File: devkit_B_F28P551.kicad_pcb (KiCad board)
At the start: 2 copper layers, 28 x 75 mm, 27 parts, among them J1 DEVKIT_C2000_ROW_A, J2 DEVKIT_C2000_ROW_B, J3 Tag-Connect-2050_10, J4 RESET, U1 TMS320F28P551SG5PM, U2 MCP1700-3302E/TT, U3 MCP1700-3302E/TT

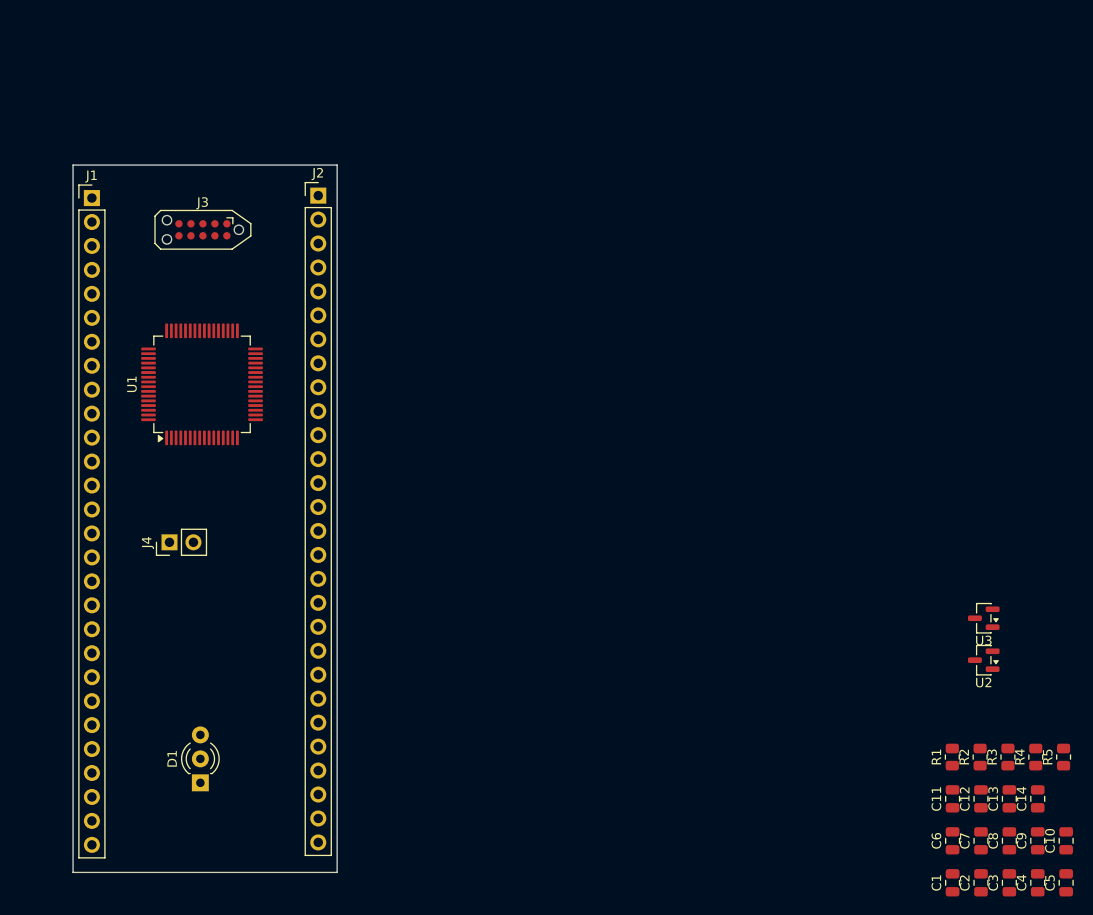
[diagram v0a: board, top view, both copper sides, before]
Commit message: Devkit B routé, sérigraphie des connecteurs 2x28 et logo
Placement/routage complet du PCB devkit B (24 empreintes, J1/J2 câblés).
Étiquettes de sérigraphie ajoutées sur les 56 broches des connecteurs
Row A/Row B (canal ADC réel, GPIO, rôle de bus générique, alimentations)
via kipy sur l'instance ouverte, plutôt que les noms spécialisés du
schéma. Logo ajouté (lib/lebel-logo) et fp-lib-table versionné.

Co-Authored-By: Claude Sonnet 5 <noreply@anthropic.com>
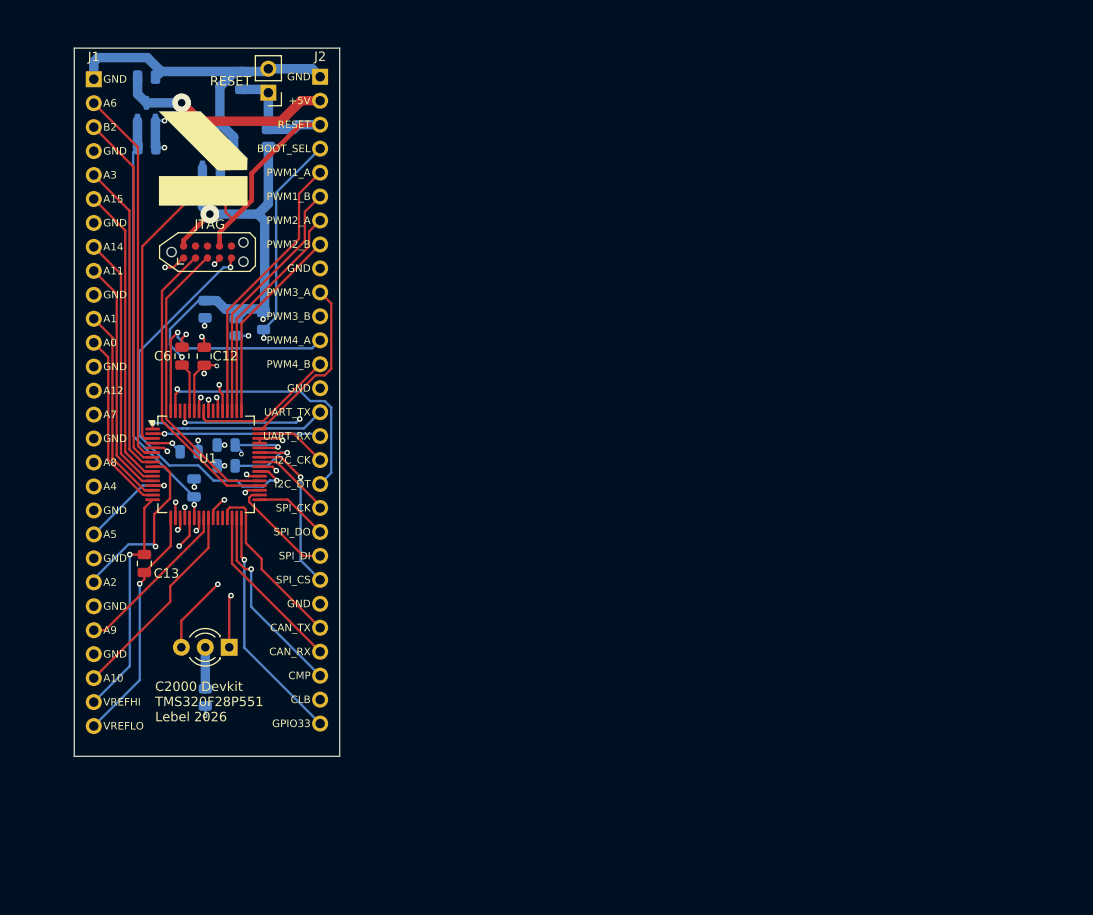
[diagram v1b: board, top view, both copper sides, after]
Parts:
- removed C7: 2u2, Capacitor_SMD:C_0805_2012Metric
- removed C9: 100n, Capacitor_SMD:C_0805_2012Metric
- removed J3: Tag-Connect-2050_10, Connector:Tag-Connect_TC2050-IDC-NL_2x05_P1.27mm_Vertical
- added G***: LOGO, lib:lebel-logo, F.Cu at (137.6, 55.8)
- added JTAG: Tag-Connect-2050_10, Connector:Tag-Connect_TC2050-IDC-NL_2x05_P1.27mm_Vertical, F.Cu at (137.8, 65.7)
- C1, C10, C11, C14, C2, C3, C4, C5, C8, J1, J2, R1, R2, R3, R4, R5, U2, U3: moved to B.Cu
- moved C3 125.2 mm to (131.3, 47.2), turned to 0 degrees
- moved C4 122.5 mm to (131.3, 54.7), turned to 0 degrees
- moved C14 113.7 mm to (141.4, 47.5)
- moved C1 112.6 mm to (138.1, 52.1), turned to 0 degrees
- moved C2 109.5 mm to (138.2, 59.6), turned to 0 degrees
- moved U3 103.8 mm to (131.3, 50.8), turned to 90 degrees
- moved C10 101.7 mm to (135.8, 86.9), turned to 0 degrees
- moved R2 100.0 mm to (144.2, 53.6), turned to -90 degrees
- moved C5 99.4 mm to (139.7, 88.4), turned to 180 degrees
- moved U2 97.6 mm to (138.2, 55.8), turned to 90 degrees
- moved C6 96.5 mm to (135.1, 76.8)
- moved R4 96.3 mm to (140.8, 73.7)
- moved C13 95.0 mm to (131.1, 98.8), turned to -90 degrees
- moved C12 94.8 mm to (137.4, 76.8)
- moved C8 94.2 mm to (136.3, 90.7)
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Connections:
- J1 pad 1: unconnected-(J1-GND-Pad1) -> GND
- J1 pad 10: unconnected-(J1-GND-Pad10) -> GND
- J1 pad 13: unconnected-(J1-GND-Pad13) -> GND
- J1 pad 16: unconnected-(J1-GND-Pad16) -> GND
- J1 pad 19: unconnected-(J1-GND-Pad19) -> GND
- J1 pad 21: unconnected-(J1-GND-Pad21) -> GND
- J1 pad 23: unconnected-(J1-GND-Pad23) -> GND
- J1 pad 4: unconnected-(J1-GND-Pad4) -> GND
- J1 pad 7: unconnected-(J1-GND-Pad7) -> GND
- J2 pad 1: unconnected-(J2-GND-Pad1) -> GND
- J2 pad 14: unconnected-(J2-GND-Pad14) -> GND
- J2 pad 9: unconnected-(J2-GND-Pad9) -> GND
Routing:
- net VDDIO: track 0.00 -> 81.9 mm, vias 0 -> 4
- net GND: track 0.00 -> 69.8 mm, vias 0 -> 15
- net ~{nRESET}: track 0.00 -> 65.4 mm
- net VDDA: track 0.00 -> 45.0 mm, vias 0 -> 1
- net JTAG_TDI: track 0.00 -> 42.8 mm, vias 0 -> 2
- net BOOT_SEL: track 0.00 -> 41.4 mm, vias 0 -> 2
- net Vin: track 0.00 -> 40.1 mm
- net Vout: track 0.00 -> 38.2 mm
- net VDD_CORE: track 0.00 -> 38.0 mm, vias 0 -> 5
- net CLB_OUT: track 0.00 -> 37.9 mm, vias 0 -> 1
- net V1: track 0.00 -> 33.7 mm
- net JTAG_TCK: track 0.00 -> 32.0 mm
- net Temp1: track 0.00 -> 32.0 mm
- net JTAG_TDO: track 0.00 -> 31.6 mm
- net LED_B: track 0.00 -> 31.3 mm, vias 0 -> 2
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- added copper zone on In2.Cu, net GND
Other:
- board size 28 x 75 mm -> 28.1 x 75.1 mm
- copper layers 2 -> 4
- board text added: "+5V"
- board text added: "A0"
- board text added: "A1"
- board text added: "A10"
- board text added: "A11"
- board text added: "A12"
- board text added: "A14"
- board text added: "A15"
- board text added: "A2"
- board text added: "A3"
- board text added: "A4"
- board text added: "A5"
- board text added: "A6"
- board text added: "A7"
- board text added: "A8"
- board text added: "A9"
- board text added: "B2"
- board text added: "BOOT_SEL"
- board text added: "C2000 Devkit TMS320F28P551 Lebel 2026"
- board text added: "CAN_RX"
- board text added: "CAN_TX"
- board text added: "CLB"
- board text added: "CMP"
- board text added: "GND"
- board text added: "GPIO33"
- board text added: "I2C_CK"
- board text added: "I2C_DT"
- board text added: "PWM1_A"
- board text added: "PWM1_B"
- board text added: "PWM2_A"
- board text added: "PWM2_B"
- board text added: "PWM3_A"
- board text added: "PWM3_B"
- board text added: "PWM4_A"
- board text added: "PWM4_B"
- board text added: "RESET"
- board text added: "SPI_CK"
- board text added: "SPI_CS"
- board text added: "SPI_DI"
- board text added: "SPI_DO"
- board text added: "UART_RX"
- board text added: "UART_TX"
- board text added: "VREFHI"
- board text added: "VREFLO"

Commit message: Corrige le chevauchement silkscreen/cuivre sur UART_RX
Etiquette raccourcie en RT_RX et clearance JTAG/masse resolue :
DRC propre (0 violation).

Co-Authored-By: Claude Sonnet 5 <noreply@anthropic.com>
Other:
- board text added: "RT_RX"
- board text removed: "UART_RX"
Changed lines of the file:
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@@
 		)
 	)
-	(gr_text "UART_RX"
+	(gr_text "RT_RX"
 		(at 148.7 85.24 0)
 		(layer "F.SilkS")

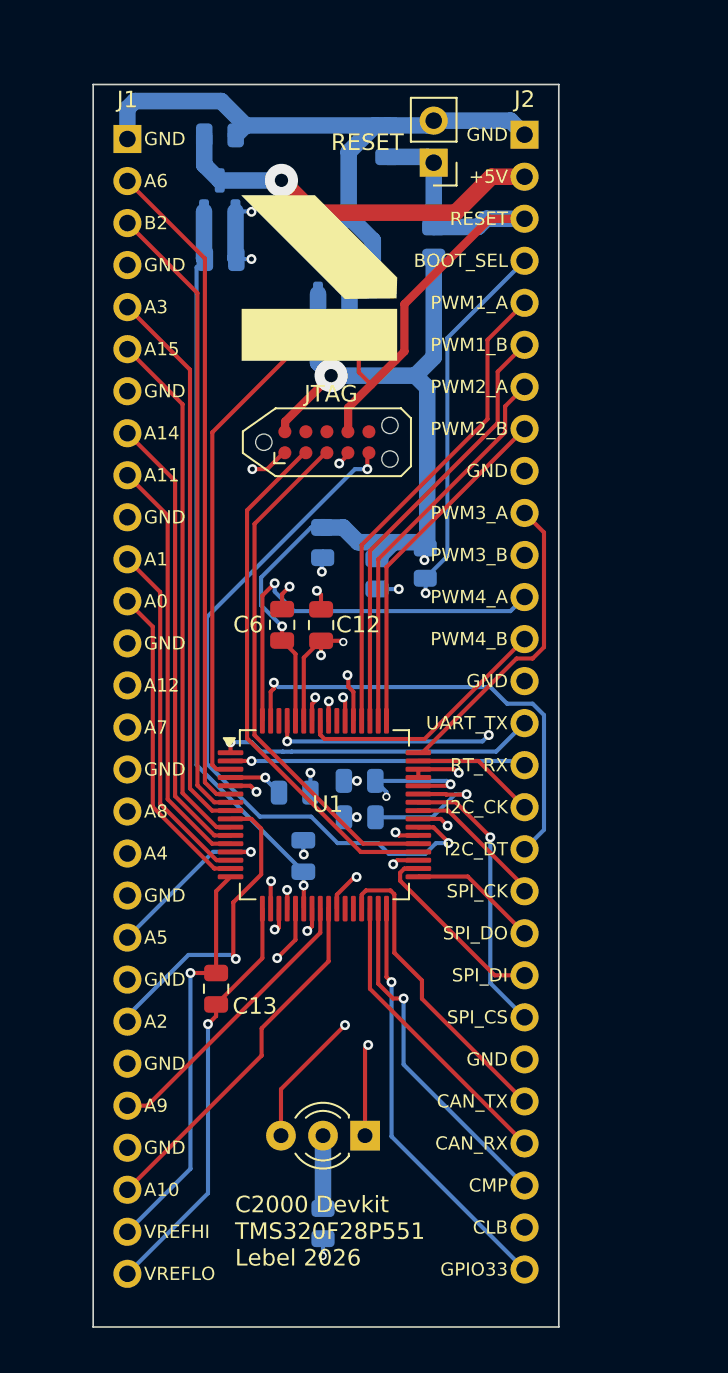
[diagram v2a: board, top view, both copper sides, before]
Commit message: Renomme les references au depot (KICAD-C2000-shield -> KICAD-C2000-devkit), suite a jour sur devkit_B_F28P551
Met a jour CLAUDE.md, README.md et doc/publier-un-projet.md apres le
renommage du depot GitHub. devkit_B_F28P551.kicad_pcb reflete le travail
de routage en cours.

Co-Authored-By: Claude Sonnet 5 <noreply@anthropic.com>
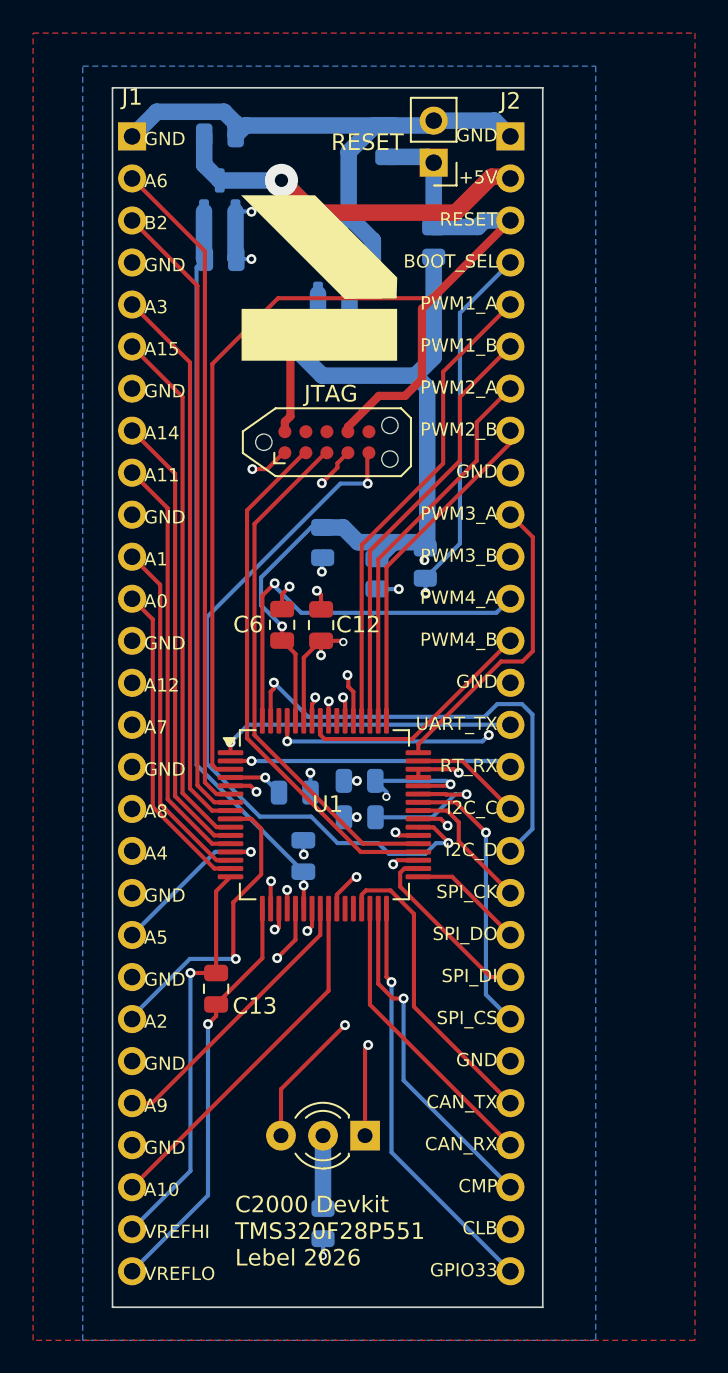
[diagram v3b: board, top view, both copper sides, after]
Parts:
- moved J2 0.86 mm to (148.8, 47.2)
- moved J1 0.32 mm to (126.0, 47.2)
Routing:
- net ~{nRESET}: track 65.4 -> 69.8 mm
- net VDDIO: track 81.9 -> 85.5 mm
- net GND: track 69.8 -> 67.1 mm
- net UART_TX: track 19.4 -> 18.0 mm
- net PWM4_A: track 25.1 -> 24.1 mm
- net PWM4_B: track 15.8 -> 14.9 mm
- net SPI_SIMO: track 7.85 -> 7.02 mm
- net I2C_SCL: track 7.58 -> 6.76 mm
- net UART_RX: track 17.9 -> 17.1 mm
- net +5V: track 29.5 -> 28.7 mm
- net I_SHUNT1_CMP: track 19.3 -> 18.6 mm
- net SPI_SOMI: track 11.6 -> 11.0 mm
- net JTAG_TDI: track 42.8 -> 43.3 mm
- added copper zone on B.Cu, net GND
- added copper zone on F.Cu, net GND
- added copper zone on In1.Cu, net GND
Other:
- board size 28.1 x 75.1 mm -> 26 x 73.7 mm
- board text added: "I2C_C"
- board text added: "I2C_D"
- board text removed: "I2C_CK"
- board text removed: "I2C_DT"

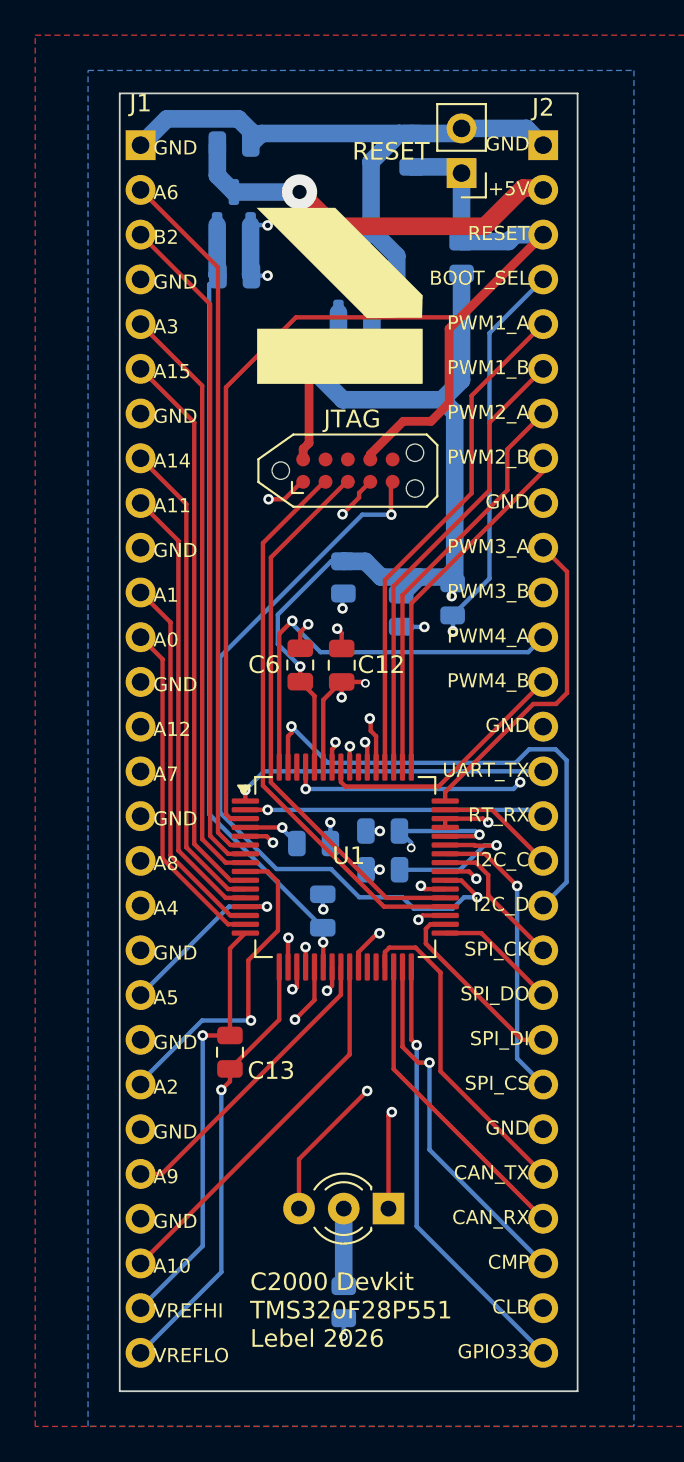
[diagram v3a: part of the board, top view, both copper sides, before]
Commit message: Ajuste le preset de via a 0.6/0.3mm et resauvegarde le PCB
Changement de reglage de projet (diametre de via 0.5->0.6mm, meme percage),
plus la resauvegarde associee du PCB par KiCad (zones de cuivre regenerees).

Co-Authored-By: Claude Sonnet 5 <noreply@anthropic.com>
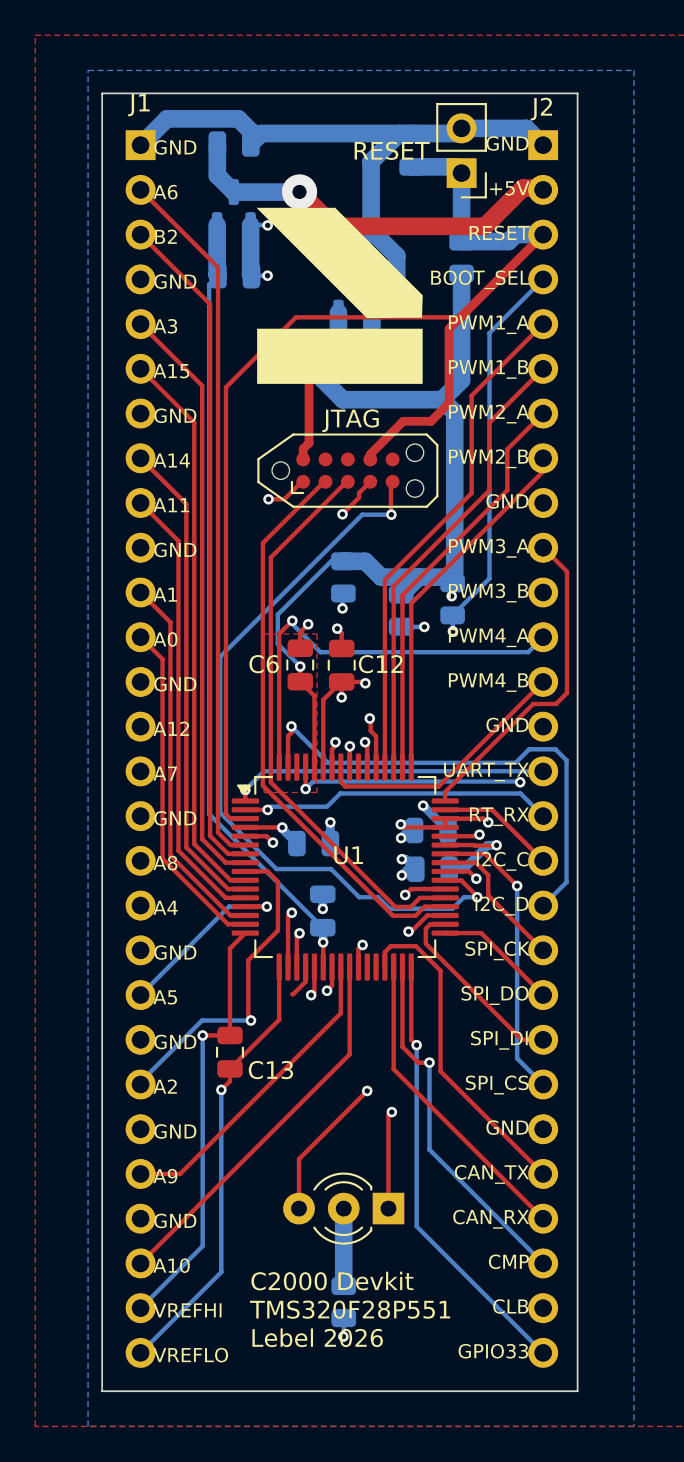
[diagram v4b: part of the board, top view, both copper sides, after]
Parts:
- moved C5 2.82 mm to (142.6, 88.4)
- moved C11 2.76 mm to (142.5, 86.2)
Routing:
- net VDD_CORE: track 38.0 -> 33.7 mm
- net ADC_11: track 16.7 -> 13.6 mm, vias 1 -> 0
- net JTAG_TMS: track 28.5 -> 31.4 mm
- net VDDIO: track 85.5 -> 82.8 mm
- net GND: track 67.1 -> 68.9 mm, vias 15 -> 17
- net BOOT_SEL: track 40.9 -> 42.7 mm
- net ADC_10: track 17.4 -> 16.0 mm
- net UART_RX: track 17.1 -> 17.8 mm
- net I_SHUNT2_MES: track 17.2 -> 17.8 mm
- added copper zone on F.Cu, net VDDIO
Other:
- board size 26 x 73.7 mm -> 27 x 73.7 mm
